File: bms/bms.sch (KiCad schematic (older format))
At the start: 10 parts

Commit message: temperature sensing
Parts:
- removed BT? (x6): Battery_Cell, symbol Device:Battery_Cell
- added J?: Conn_01x02_Female, symbol Connector:Conn_01x02_Female
- added J? (x2): Conn_01x03_Female, symbol Connector:Conn_01x03_Female
- added J?: Barrel_Jack_Switch, symbol Connector:Barrel_Jack_Switch
- added R? (x3): R, symbol Device:R
- added TH? (x3): Thermistor_NTC_US, symbol Device:Thermistor_NTC_US
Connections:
- net labels added: 12V, BT1, BT2, BT3, BT4, BT5, BT6, GND, SD, Switch, TH, TH1, TH2, TH3
- wire segments 5 -> 23
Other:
- moved on the sheet: D?

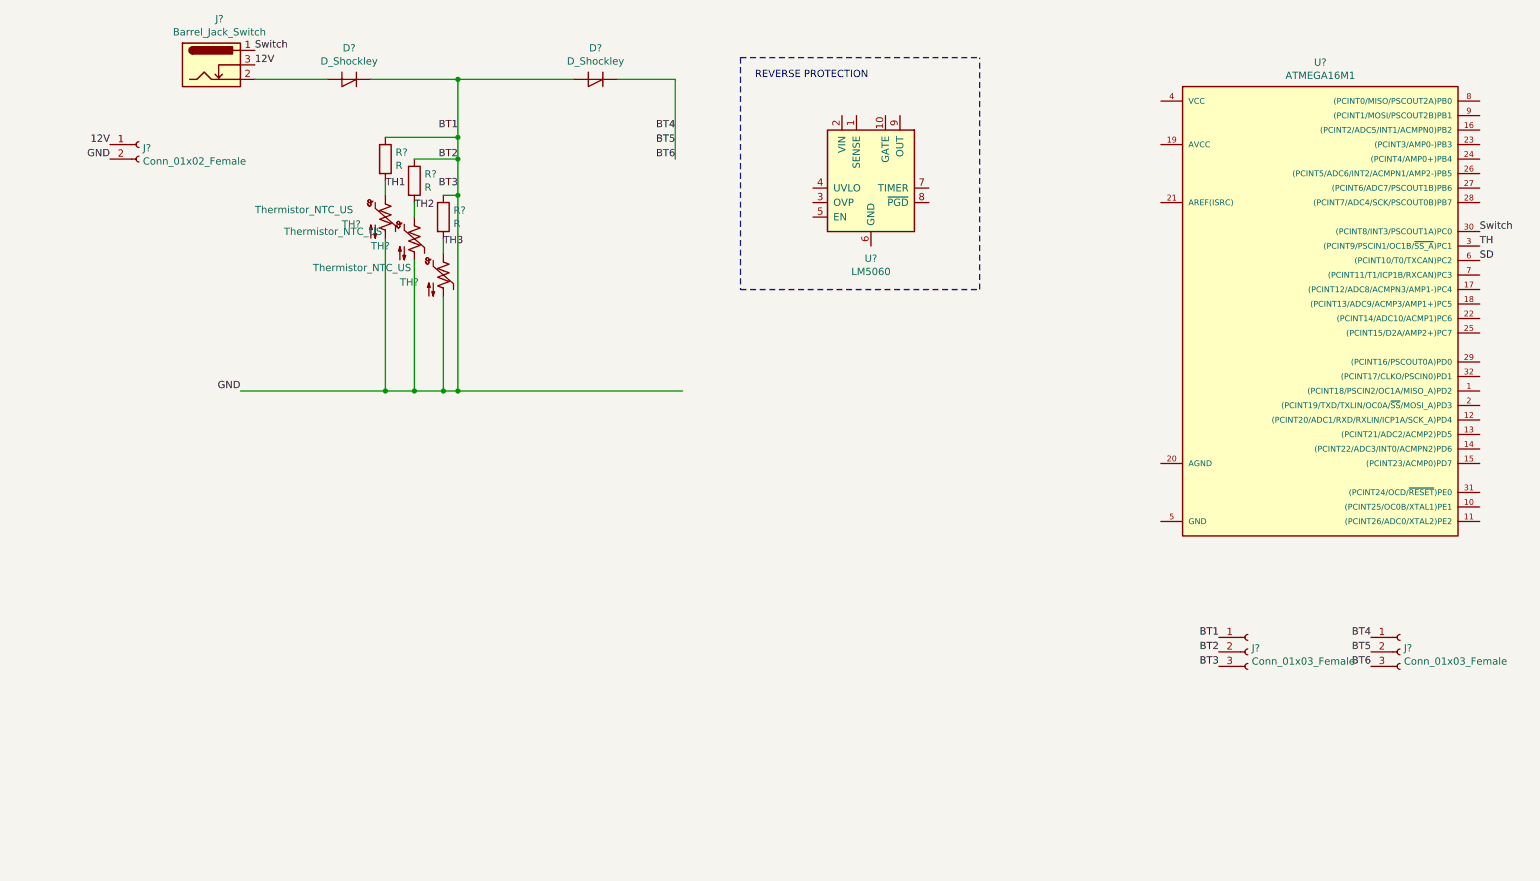
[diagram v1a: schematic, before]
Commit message: passive charge redistribution and temp monitoring
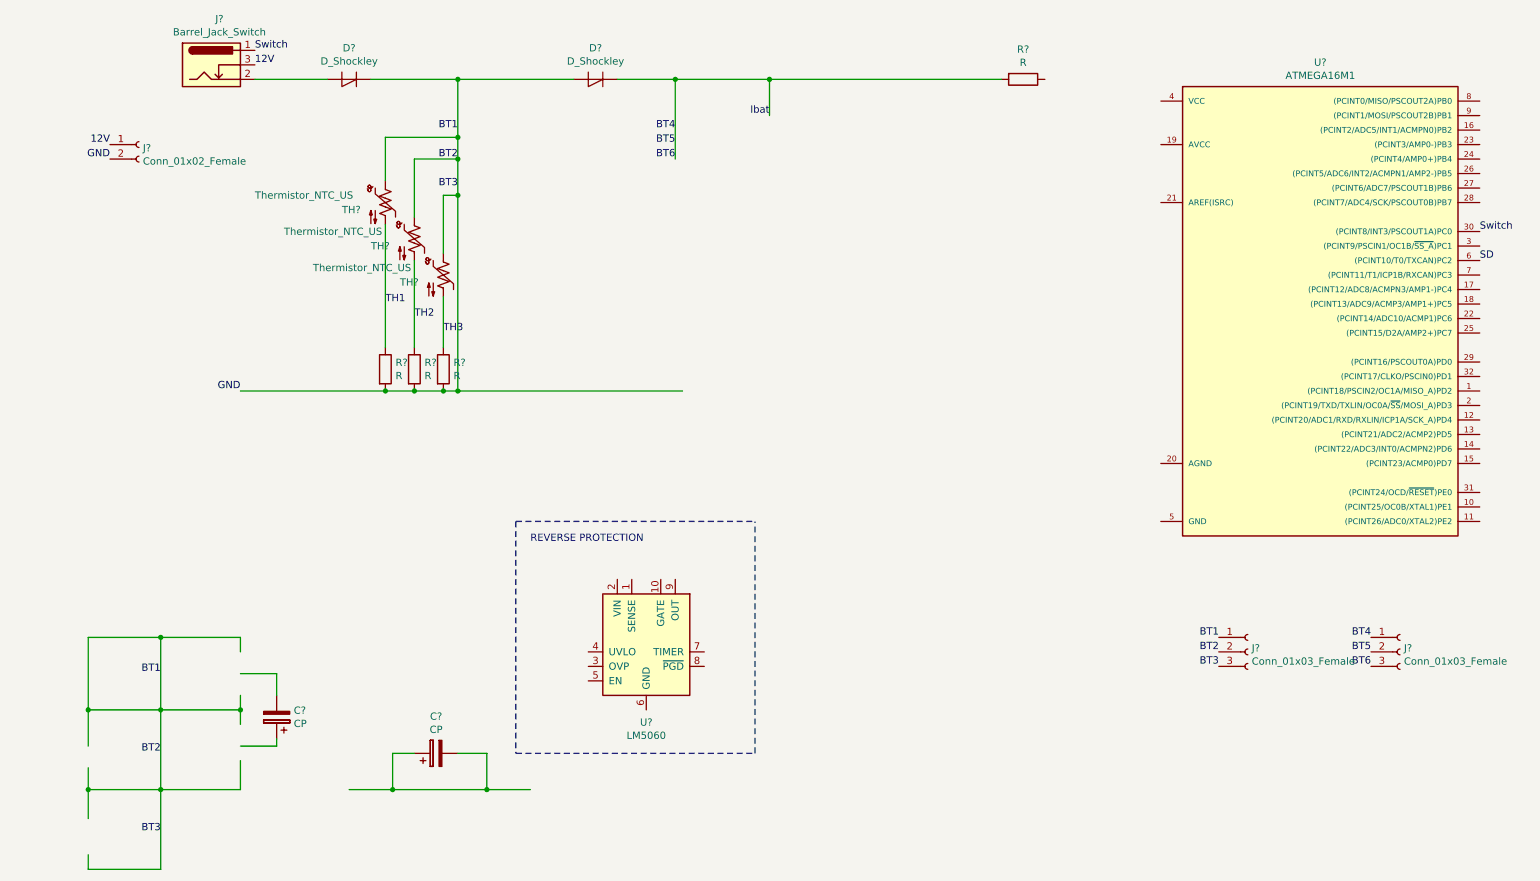
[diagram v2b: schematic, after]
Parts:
- added C? (x2): CP, symbol Device:CP
- added R?: R, symbol Device:R
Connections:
- net labels added: Ibat
- net labels removed: TH
- wire segments 23 -> 56
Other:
- moved on the sheet: R?, TH?, U?
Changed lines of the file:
@@
 L Power_Management:LM5060 U?
 U 1 1 5D97B396
-P 6350 1650
-F 0 "U?" H 6350 1064 50  0000 C CNN
-F 1 "LM5060" H 6350 973 50  0000 C CNN
-F 2 "Package_SO:MSOP-10_3x3mm_P0.5mm" H 6550 1050 50  0001 C CNN
-F 3 "http://www.ti.com/lit/ds/symlink/lm5060.pdf" H 6350 2100 50  0001 C CNN
-	1    6350 1650
-	1    0    0    -1
-$EndComp
-Text Notes 5550 1000 0    50   ~ 0
+P 4800 4850
+F 0 "U?" H 4800 4264 50  0000 C CNN
+F 1 "LM5060" H 4800 4173 50  0000 C CNN
+F 2 "Package_SO:MSOP-10_3x3mm_P0.5mm" H 5000 4250 50  0001 C CNN
+F 3 "http://www.ti.com/lit/ds/symlink/lm5060.pdf" H 4800 5300 50  0001 C CNN
+	1    4800 4850
+	1    0    0    -1
+$EndComp
+Text Notes 4000 4200 0    50   ~ 0
 REVERSE PROTECTION
 Wire Notes Line
-	5450 850  5450 2450
+	3900 4050 3900 5650
 Wire Notes Line
-	5450 2450 7100 2450
+	3900 5650 5550 5650
 Wire Notes Line
-	7100 2450 7100 850
+	5550 5650 5550 4050
 Wire Notes Line
-	5450 850  7100 850
+	3900 4050 5550 4050
 Wire Wire Line
 	2100 1000 2600 1000
@@
 L Device:Thermistor_NTC_US TH?
 U 1 1 5DAE42F9
-P 3000 1950
-F 0 "TH?" H 2700 1900 50  0000 L CNN
-F 1 "Thermistor_NTC_US" H 2100 2000 50  0000 L CNN
-F 2 "" H 3000 2000 50  0001 C CNN
-F 3 "~" H 3000 2000 50  0001 C CNN
-	1    3000 1950
-	1    0    0    -1
-$EndComp
-Text Label 10550 2150 0    50   ~ 0
-TH
+P 3000 1850
+F 0 "TH?" H 2700 1800 50  0000 L CNN
+F 1 "Thermistor_NTC_US" H 2100 1900 50  0000 L CNN
+F 2 "" H 3000 1900 50  0001 C CNN
+F 3 "~" H 3000 1900 50  0001 C CNN
+	1    3000 1850
+	1    0    0    -1
+$EndComp
 $Comp
 L Device:R R?
 U 1 1 5DAE50A0
-P 3000 1550
-F 0 "R?" H 3070 1596 50  0000 L CNN
-F 1 "R" H 3070 1505 50  0000 L CNN
-F 2 "" V 2930 1550 50  0001 C CNN
-F 3 "~" H 3000 1550 50  0001 C CNN
-	1    3000 1550
-	1    0    0    -1
-$EndComp
-Text Label 3000 1750 0    50   ~ 0
+P 3000 3000
+F 0 "R?" H 3070 3046 50  0000 L CNN
+F 1 "R" H 3070 2955 50  0000 L CNN
+F 2 "" V 2930 3000 50  0001 C CNN
+F 3 "~" H 3000 3000 50  0001 C CNN
+	1    3000 3000
+	1    0    0    -1
+$EndComp
+Text Label 3000 2550 0    50   ~ 0
 TH1
-Wire Wire Line
-	3000 1800 3000 1700
 Wire Wire Line
 	3000 1400 3500 1400
@@
 Wire Wire Line
 	3500 1400 3500 1550
-Wire Wire Line
-	2000 3150 3000 3150
-Wire Wire Line
-	3000 2100 3000 3150
-Connection ~ 3000 3150
-Wire Wire Line
-	3000 3150 3200 3150
 $Comp
 L Device:Thermistor_NTC_US TH?
@@
 	1    0    0    -1
 $EndComp
-$Comp
-L Device:R R?
-U 1 1 5DAE5AF1
-P 3200 1700
-F 0 "R?" H 3270 1746 50  0000 L CNN
-F 1 "R" H 3270 1655 50  0000 L CNN
-F 2 "" V 3130 1700 50  0001 C CNN
-F 3 "~" H 3200 1700 50  0001 C CNN
-	1    3200 1700
-	1    0    0    -1
-$EndComp
-Text Label 3200 1900 0    50   ~ 0
+Text Label 3200 2650 0    50   ~ 0
 TH2
-Wire Wire Line
-	3200 1950 3200 1850
 $Comp
 L Device:Thermistor_NTC_US TH?
@@
 	1    0    0    -1
 $EndComp
+Text Label 3400 2750 0    50   ~ 0
+TH3
+Wire Wire Line
+	3200 1550 3500 1550
+Connection ~ 3500 1550
+Wire Wire Line
+	3500 1550 3500 1800
+Connection ~ 3500 3150
+Wire Wire Line
+	3500 3150 5050 3150
+Wire Wire Line
+	3400 1800 3500 1800
+Connection ~ 3500 1800
+Wire Wire Line
+	3500 1800 3500 3150
+Text Label 10550 2250 0    50   ~ 0
+SD
+Connection ~ 5000 1000
+Wire Wire Line
+	5000 1000 5650 1000
+Wire Wire Line
+	5650 1000 5650 1250
+Connection ~ 5650 1000
+Wire Wire Line
+	5650 1000 7250 1000
+Text Label 5650 1250 2    50   ~ 0
+Ibat
+Wire Wire Line
+	2000 3150 3000 3150
+Connection ~ 3000 3150
 $Comp
 L Device:R R?
 U 1 1 5DAE5C61
-P 3400 1950
-F 0 "R?" H 3470 1996 50  0000 L CNN
-F 1 "R" H 3470 1905 50  0000 L CNN
-F 2 "" V 3330 1950 50  0001 C CNN
-F 3 "~" H 3400 1950 50  0001 C CNN
-	1    3400 1950
-	1    0    0    -1
-$EndComp
-Text Label 3400 2150 0    50   ~ 0
-TH3
-Wire Wire Line
-	3400 2200 3400 2100
-Wire Wire Line
-	3200 1550 3500 1550
-Connection ~ 3500 1550
-Wire Wire Line
-	3500 1550 3500 1800
-Connection ~ 3500 3150
-Wire Wire Line
-	3500 3150 5050 3150
-Wire Wire Line
-	3400 1800 3500 1800
-Connection ~ 3500 1800
-Wire Wire Line
-	3500 1800 3500 3150
-Wire Wire Line
-	3200 2250 3200 3150
+P 3400 3000
+F 0 "R?" H 3470 3046 50  0000 L CNN
+F 1 "R" H 3470 2955 50  0000 L CNN
+F 2 "" V 3330 3000 50  0001 C CNN
+F 3 "~" H 3400 3000 50  0001 C CNN
+	1    3400 3000
+	1    0    0    -1
+$EndComp
+$Comp
+L Device:R R?
+U 1 1 5DAE5AF1
+P 3200 3000
+F 0 "R?" H 3270 3046 50  0000 L CNN
+F 1 "R" H 3270 2955 50  0000 L CNN
+F 2 "" V 3130 3000 50  0001 C CNN
+F 3 "~" H 3200 3000 50  0001 C CNN
+	1    3200 3000
+	1    0    0    -1
+$EndComp
+Wire Wire Line
+	3000 3150 3200 3150
+Connection ~ 3400 3150
+Wire Wire Line
+	3400 3150 3500 3150
 Connection ~ 3200 3150
 Wire Wire Line
 	3200 3150 3400 3150
 Wire Wire Line
-	3400 2500 3400 3150
-Connection ~ 3400 3150
-Wire Wire Line
-	3400 3150 3500 3150
-Text Label 10550 2250 0    50   ~ 0
-SD
+	3000 1400 3000 1700
+Wire Wire Line
+	3200 1550 3200 1950
+Wire Wire Line
+	3400 1800 3400 2200
+Wire Wire Line
+	3200 2250 3200 2850
+Wire Wire Line
+	3400 2500 3400 2850
+Wire Wire Line
+	3000 2000 3000 2850
+$Comp
+L Device:R R?
+U 1 1 5DB7AE6F
+P 7400 1000
+F 0 "R?" V 7193 1000 50  0000 C CNN
+F 1 "R" V 7284 1000 50  0000 C CNN
+F 2 "" V 7330 1000 50  0001 C CNN
+F 3 "~" H 7400 1000 50  0001 C CNN
+	1    7400 1000
+	0    1    1    0
+$EndComp
+Wire Wire Line
+	3500 5650 3700 5650
+Wire Wire Line
+	3700 5650 3700 5900
+Wire Wire Line
+	3200 5650 3050 5650
+Wire Wire Line
+	3050 5650 3050 5900
+Wire Wire Line
+	2750 5900 3050 5900
+Connection ~ 3050 5900
+Wire Wire Line
+	3050 5900 3700 5900
+Connection ~ 3700 5900
+Wire Wire Line
+	3700 5900 4000 5900
+$Comp
+L Device:CP C?
+U 1 1 5DBDC541
+P 3350 5650
+F 0 "C?" V 3605 5650 50  0000 C CNN
+F 1 "CP" V 3514 5650 50  0000 C CNN
+F 2 "" H 3388 5500 50  0001 C CNN
+F 3 "~" H 3350 5650 50  0001 C CNN
+	1    3350 5650
+	0    -1   -1   0
+$EndComp
+Wire Wire Line
+	2250 5550 2250 5600
+Wire Wire Line
+	2250 5600 2000 5600
+Wire Wire Line
+	2250 5250 2250 5100
+Wire Wire Line
+	2250 5100 2000 5100
+$Comp
+L Device:CP C?
+U 1 1 5DBDCD8D
+P 2250 5400
+F 0 "C?" H 2132 5354 50  0000 R CNN
+F 1 "CP" H 2132 5445 50  0000 R CNN
+F 2 "" H 2288 5250 50  0001 C CNN
+F 3 "~" H 2250 5400 50  0001 C CNN
+	1    2250 5400
+	-1   0    0    1
+$EndComp
+Wire Wire Line
+	1450 5350 2000 5350
+Text Label 1450 5100 2    50   ~ 0
+BT1
+Wire Wire Line
+	2000 5250 2000 5350
+Connection ~ 2000 5350
+Wire Wire Line
+	2000 5350 2000 5450
+Text Label 1450 5650 2    50   ~ 0
+BT2
+Wire Wire Line
+	1450 5900 2000 5900
+Connection ~ 1450 5350
+Wire Wire Line
+	2000 5700 2000 5900
+Text Label 1450 6200 2    50   ~ 0
+BT3
+Connection ~ 1450 5900
+Wire Wire Line
+	1450 4850 1450 5350
+Wire Wire Line
+	1450 5900 950  5900
+Wire Wire Line
+	1450 5350 950  5350
+Wire Wire Line
+	1450 6450 950  6450
+Wire Wire Line
+	950  6450 950  6350
+Wire Wire Line
+	950  6100 950  5900
+Connection ~ 950  5900
+Wire Wire Line
+	950  5900 950  5750
+Connection ~ 950  5350
+Wire Wire Line
+	950  4850 1450 4850
+Wire Wire Line
+	1450 5900 1450 6450
+Wire Wire Line
+	950  5350 950  4850
+Wire Wire Line
+	1450 5350 1450 5900
+Wire Wire Line
+	950  5350 950  5600
+Connection ~ 1450 4850
+Wire Wire Line
+	1450 4850 2000 4850
+Wire Wire Line
+	2000 4850 2000 4950
 $EndSCHEMATC

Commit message: started charging and balancing
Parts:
- removed C?: CP, symbol Device:CP
- removed D? (x2): D_Shockley, symbol Device:D_Shockley
- removed U?: LM5060, Package_SO:MSOP-10_3x3mm_P0.5mm, symbol Power_Management:LM5060
- added C?: CP, symbol Device:CP
- added D? (x3): D, symbol Device:D
- added D? (x3): D_Schottky, symbol Device:D_Schottky
- added Q1: 2N3904, Package_TO_SOT_THT:TO-92_Inline, symbol Transistor_BJT:2N3904
- added R? (x7): R, symbol Device:R
- added TH? (x3): Thermistor_NTC_US, symbol Device:Thermistor_NTC_US
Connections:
- net labels added: TH4, TH5, TH6
- net labels removed: Ibat
- wire segments 56 -> 86
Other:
- note added: "Bias current"
- note added: "Passive Charge Redistribution"
- note removed: "REVERSE PROTECTION"
- moved on the sheet: J?

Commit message: charging circuit
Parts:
- removed U?: ATMEGA16M1, footprints:TQFP-32_7x7mm_Pitch0.8mm, symbol formula:ATMEGA16M1
- added C?: C_Small, symbol Device:C_Small
- added C?: CP_Small, symbol Device:CP_Small
- added D?: D_Schottky, symbol Device:D_Schottky
- added Q?: Q_NJFET_DGS, symbol Device:Q_NJFET_DGS
- added Q?: Q_PJFET_DGS, symbol Device:Q_PJFET_DGS
- added R?: R, symbol Device:R
- added U?: ATSAML21J18B-AUT, Package_QFP:TQFP-64_10x10mm_P0.5mm, symbol MCU_Microchip_SAML:ATSAML21J18B-AUT
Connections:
- wire segments 86 -> 99
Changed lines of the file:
@@
 $EndDescr
-$Comp
-L formula:ATMEGA16M1 U?
-U 1 1 5D97ADEC
-P 9450 2850
-F 0 "U?" H 9450 4817 50  0000 C CNN
-F 1 "ATMEGA16M1" H 9450 4726 50  0000 C CNN
-F 2 "footprints:TQFP-32_7x7mm_Pitch0.8mm" H 9450 2850 50  0001 C CIN
-F 3 "http://ww1.microchip.com/downloads/en/DeviceDoc/Atmel-8209-8-bit%20AVR%20ATmega16M1-32M1-64M1_Datasheet.pdf" H 8500 4680 50  0001 C CNN
-F 4 "DK" H 9450 2850 60  0001 C CNN "MFN"
-F 5 "ATMEGA16M1-AU-ND" H 9450 2850 60  0001 C CNN "MPN"
-F 6 "https://www.digikey.com/product-detail/en/atmel/ATMEGA16M1-AU/ATMEGA16M1-AU-ND/2271208" H 8900 5080 60  0001 C CNN "PurchasingLink"
-	1    9450 2850
-	1    0    0    -1
-$EndComp
 $Comp
 L Connector:Conn_01x02_Female J?
@@
 Text Label 5700 1800 2    50   ~ 0
 BT6
-Text Label 3250 3150 2    50   ~ 0
-GND
 $Comp
 L Device:Thermistor_NTC_US TH?
@@
 Wire Wire Line
 	1800 1000 1800 1300
-Connection ~ 1800 1000
-Wire Wire Line
-	1800 1000 2600 1000
 Connection ~ 1800 1300
 $Comp
@@
 Wire Wire Line
 	1300 1550 1950 1550
-Wire Wire Line
-	3650 1000 3250 1000
-Text Label 3250 1000 2    50   ~ 0
-12V
 Connection ~ 4050 3150
-Wire Wire Line
-	3250 3150 4050 3150
 Wire Wire Line
 	5350 1000 5700 1000
@@
 	-1   0    0    1
 $EndComp
+$Comp
+L MCU_Microchip_SAML:ATSAML21J18B-AUT U?
+U 1 1 5DCF31A5
+P 9300 2650
+F 0 "U?" H 9300 664 50  0000 C CNN
+F 1 "ATSAML21J18B-AUT" H 9300 573 50  0000 C CNN
+F 2 "Package_QFP:TQFP-64_10x10mm_P0.5mm" H 10500 4450 50  0001 C CNN
+F 3 "http://ww1.microchip.com/downloads/en/DeviceDoc/60001477A.pdf" H 9300 2650 50  0001 C CNN
+	1    9300 2650
+	1    0    0    -1
+$EndComp
+$Comp
+L Device:R R?
+U 1 1 5DCF5403
+P 2250 2200
+F 0 "R?" H 2320 2246 50  0001 L CNN
+F 1 "R" H 2320 2155 50  0000 L CNN
+F 2 "" V 2180 2200 50  0001 C CNN
+F 3 "~" H 2250 2200 50  0001 C CNN
+	1    2250 2200
+	1    0    0    -1
+$EndComp
+Connection ~ 2250 2050
+$Comp
+L Device:Q_NJFET_DGS Q?
+U 1 1 5DCF7689
+P 2150 2800
+F 0 "Q?" H 2341 2800 50  0000 L CNN
+F 1 "Q_NJFET_DGS" H 2341 2755 50  0001 L CNN
+F 2 "" H 2350 2900 50  0001 C CNN
+F 3 "~" H 2150 2800 50  0001 C CNN
+	1    2150 2800
+	1    0    0    -1
+$EndComp
+Wire Wire Line
+	2250 2600 2250 2350
+Connection ~ 2250 2350
+Wire Wire Line
+	2250 3000 2250 3150
+Wire Wire Line
+	2250 3150 1800 3150
+Connection ~ 1800 3150
+Connection ~ 2250 3150
+$Comp
+L Device:Q_PJFET_DGS Q?
+U 1 1 5DD0060A
+P 2250 1100
+F 0 "Q?" V 2486 1100 50  0000 C CNN
+F 1 "Q_PJFET_DGS" V 2577 1100 50  0001 C CNN
+F 2 "" H 2450 1200 50  0001 C CNN
+F 3 "~" H 2250 1100 50  0001 C CNN
+	1    2250 1100
+	0    -1   -1   0
+$EndComp
+Connection ~ 2250 1300
+Wire Wire Line
+	1800 1000 2050 1000
+Connection ~ 1800 1000
+$Comp
+L Device:D_Schottky D?
+U 1 1 5DD0C2EB
+P 2750 1000
+F 0 "D?" V 2750 1079 50  0001 L CNN
+F 1 "D_Schottky" V 2795 1079 50  0001 L CNN
+F 2 "" H 2750 1000 50  0001 C CNN
+F 3 "~" H 2750 1000 50  0001 C CNN
+	1    2750 1000
+	-1   0    0    1
+$EndComp
+Wire Wire Line
+	2450 1000 2600 1000
+$Comp
+L Device:C_Small C?
+U 1 1 5DD0EAEB
+P 2750 1950
+F 0 "C?" H 2842 1950 50  0000 L CNN
+F 1 "C_Small" H 2842 1905 50  0001 L CNN
+F 2 "" H 2750 1950 50  0001 C CNN
+F 3 "~" H 2750 1950 50  0001 C CNN
+	1    2750 1950
+	1    0    0    -1
+$EndComp
+Wire Wire Line
+	2250 2050 2750 2050
+Wire Wire Line
+	2750 2050 3050 2050
+Connection ~ 2750 2050
+Wire Wire Line
+	2250 2350 3050 2350
+Wire Wire Line
+	2900 1000 3050 1000
+Wire Wire Line
+	3050 1000 3050 1300
+Connection ~ 3050 1000
+Wire Wire Line
+	3050 1000 3500 1000
+Wire Wire Line
+	2250 3150 3500 3150
+Wire Wire Line
+	3500 1000 3500 2750
+Connection ~ 3500 1000
+Wire Wire Line
+	3500 1000 3650 1000
+$Comp
+L Device:CP_Small C?
+U 1 1 5DD2011C
+P 3500 2850
+F 0 "C?" H 3588 2850 50  0000 L CNN
+F 1 "CP_Small" H 3588 2805 50  0001 L CNN
+F 2 "" H 3500 2850 50  0001 C CNN
+F 3 "~" H 3500 2850 50  0001 C CNN
+	1    3500 2850
+	1    0    0    -1
+$EndComp
+Wire Wire Line
+	3500 2950 3500 3150
+Connection ~ 3500 3150
+Wire Wire Line
+	3500 3150 4050 3150
 $EndSCHEMATC
